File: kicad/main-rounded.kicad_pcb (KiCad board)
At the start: 2 copper layers, 130.7 x 94.9 mm, 40 parts

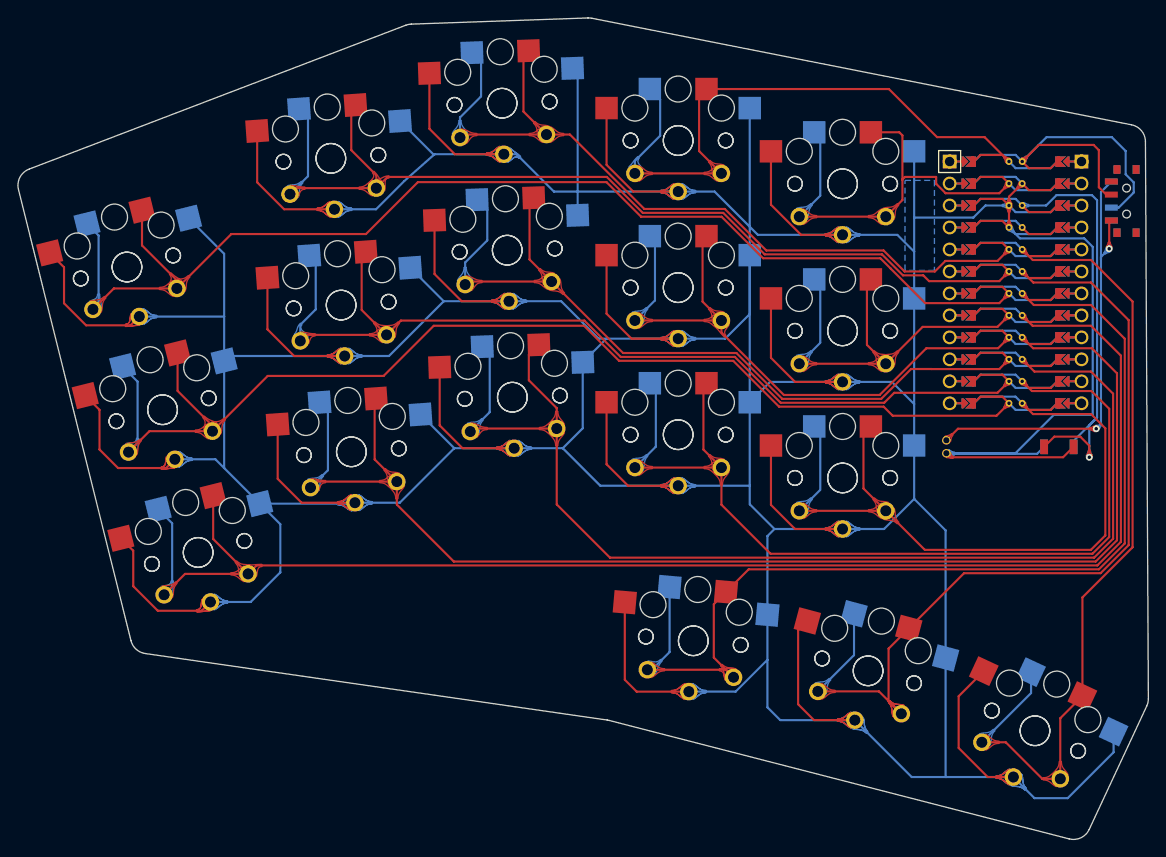
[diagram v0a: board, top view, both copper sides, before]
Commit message: feat: rounded tracks
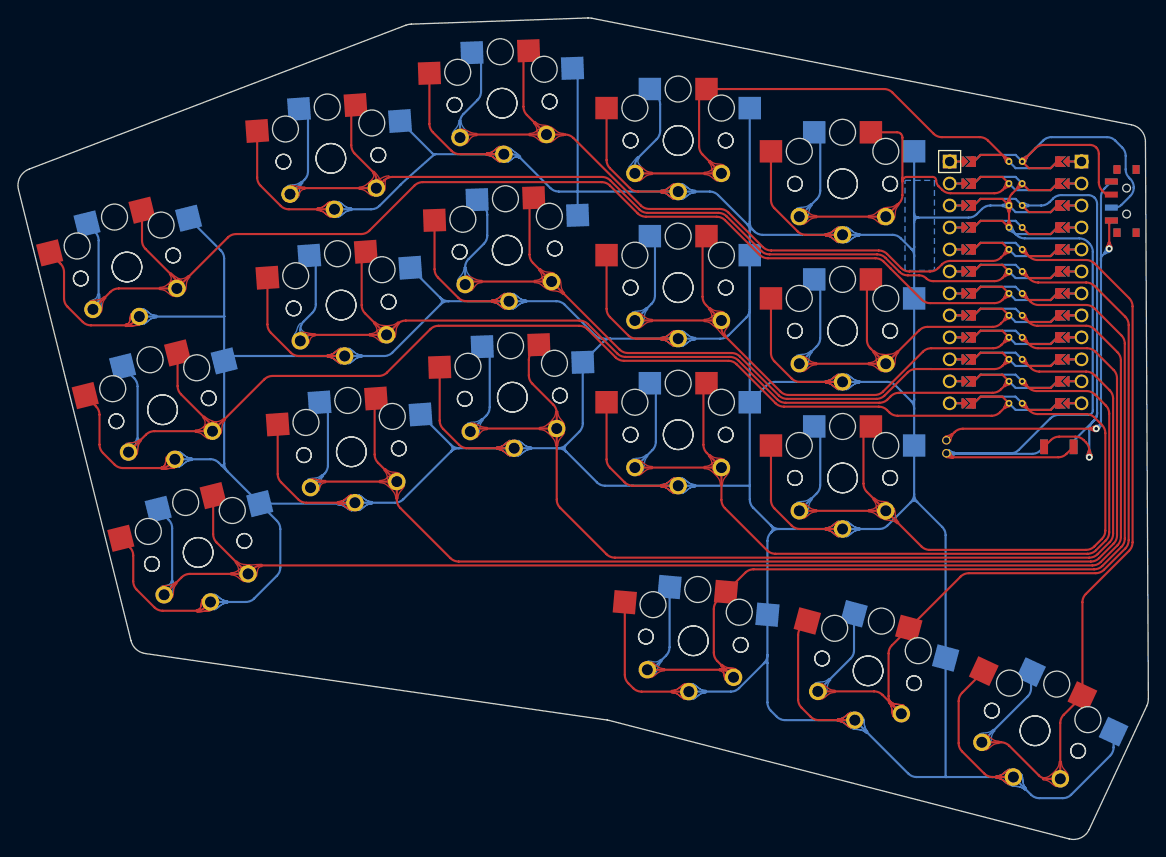
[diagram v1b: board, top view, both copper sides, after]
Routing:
- net GND: track 959.2 -> 966.4 mm
- net P19: track 118.2 -> 117.0 mm
- net P9: track 133.8 -> 132.9 mm
- net P2: track 90.7 -> 89.9 mm
- net P8: track 108.0 -> 107.2 mm
- net P14: track 136.5 -> 135.7 mm
- net RAW: track 37.7 -> 37.0 mm
- net P7: track 91.6 -> 91.0 mm
- net P20: track 102.9 -> 102.3 mm
- net P15: track 152.1 -> 151.4 mm
- net P16: track 108.8 -> 108.2 mm
- net P21: track 95.2 -> 94.6 mm
- net P10: track 81.1 -> 80.6 mm
